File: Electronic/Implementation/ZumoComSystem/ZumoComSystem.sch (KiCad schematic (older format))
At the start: 9 parts, among them J1 Conn_02x13_Odd_Even, J2 USB_A, J3 Conn_02x07_Odd_Even, J4 Conn_02x07_Odd_Even, J5 Conn_02x13_Odd_Even, P1 USB_C_Plug, U1 ESP32-WROOM-32

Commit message: add vertical usb ports (!!!ATTENTION: wrong footprints!!!) only for demonstration
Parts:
- J2: footprint Connector_USB:USB_A_Wuerth_61400826021_Horizontal_Stacked -> footprints:USB_A_Molex_105057_Vertical_2
- P1: footprint Connector_USB:USB_C_Receptacle_GCT_USB4085 -> footprints:USB_C_Receptacle_JAE_DX07S024WJ3R400
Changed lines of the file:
@@
 F 0 "P1" H 9757 3117 50  0000 C CNN
 F 1 "USB_C_Plug" H 9757 3026 50  0000 C CNN
-F 2 "Connector_USB:USB_C_Receptacle_GCT_USB4085" H 9800 1850 50  0001 C CNN
+F 2 "footprints:USB_C_Receptacle_JAE_DX07S024WJ3R400" H 9800 1850 50  0001 C CNN
 F 3 "https://www.usb.org/sites/default/files/documents/usb_type-c.zip" H 9800 1850 50  0001 C CNN
 	1    9650 1850
@@
 F 0 "J2" H 1807 6667 50  0000 C CNN
 F 1 "USB_A" H 1807 6576 50  0000 C CNN
-F 2 "Connector_USB:USB_A_Wuerth_61400826021_Horizontal_Stacked" H 1900 6150 50  0001 C CNN
+F 2 "footprints:USB_A_Molex_105057_Vertical_2" H 1900 6150 50  0001 C CNN
 F 3 " ~" H 1900 6150 50  0001 C CNN
 	1    1750 6200

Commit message: Electronic -> Schematic -> create hierarchical structure, add USB_MAX, add Regulators
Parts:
- removed BT1, BT2: Battery_Cell, footprints:BAT_1043, symbol Device:Battery_Cell
- removed J1, J5: Conn_02x13_Odd_Even, Connector_PinHeader_2.54mm:PinHeader_2x13_P2.54mm_Vertical, symbol Connector_Generic:Conn_02x13_Odd_Even
- removed J2: USB_A, footprints:USB_A_Molex_105057_Vertical_2, symbol Connector:USB_A
- removed J3: Conn_02x07_Odd_Even, Connector_PinSocket_2.54mm:PinSocket_2x07_P2.54mm_Vertical, symbol Connector_Generic:Conn_02x07_Odd_Even
- removed J4: Conn_02x07_Odd_Even, Connector_PinHeader_2.54mm:PinHeader_2x07_P2.54mm_Vertical, symbol Connector_Generic:Conn_02x07_Odd_Even
- removed P1: USB_C_Plug, footprints:USB_C_Receptacle_JAE_DX07S024WJ3R400, symbol Connector:USB_C_Plug
- removed U1: ESP32-WROOM-32, RF_Module:ESP32-WROOM-32, symbol RF_Module:ESP32-WROOM-32
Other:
- note removed: "Display"
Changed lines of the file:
@@
 $Descr A4 11693 8268
 encoding utf-8
-Sheet 1 1
+Sheet 1 7
 Title "Zumo Communication System"
-Date "2021-05-14"
+Date "2021-06-11"
 Rev "V1.0"
 Comp "NewTec GmbH"
-Comment1 "Reyes, Gabryel"
-Comment2 "Schneider, Niklas"
+Comment1 "Schneider, Niklas"
+Comment2 ""
 Comment3 ""
 Comment4 ""
 $EndDescr
-$Comp
-L Connector_Generic:Conn_02x13_Odd_Even J1
-U 1 1 609EB143
-P 1750 4700
-F 0 "J1" H 1800 5517 50  0000 C CNN
-F 1 "Conn_02x13_Odd_Even" H 1800 5426 50  0000 C CNN
-F 2 "Connector_PinHeader_2.54mm:PinHeader_2x13_P2.54mm_Vertical" H 1750 4700 50  0001 C CNN
-F 3 "~" H 1750 4700 50  0001 C CNN
-	1    1750 4700
-	1    0    0    -1
-$EndComp
-$Comp
-L Connector_Generic:Conn_02x13_Odd_Even J5
-U 1 1 609F337D
-P 9750 4700
-F 0 "J5" H 9800 5517 50  0000 C CNN
-F 1 "Conn_02x13_Odd_Even" H 9800 5426 50  0000 C CNN
-F 2 "Connector_PinHeader_2.54mm:PinHeader_2x13_P2.54mm_Vertical" H 9750 4700 50  0001 C CNN
-F 3 "~" H 9750 4700 50  0001 C CNN
-	1    9750 4700
-	1    0    0    -1
-$EndComp
-$Comp
-L Connector_Generic:Conn_02x07_Odd_Even J4
-U 1 1 609FB3EF
-P 5950 2450
-F 0 "J4" V 6046 2062 50  0000 R CNN
-F 1 "Conn_02x07_Odd_Even" V 5955 2062 50  0000 R CNN
-F 2 "Connector_PinHeader_2.54mm:PinHeader_2x07_P2.54mm_Vertical" H 5950 2450 50  0001 C CNN
-F 3 "~" H 5950 2450 50  0001 C CNN
-	1    5950 2450
-	0    -1   -1   0
-$EndComp
-$Comp
-L Connector_Generic:Conn_02x07_Odd_Even J3
-U 1 1 609FDC66
-P 5950 1550
-F 0 "J3" V 6046 1162 50  0000 R CNN
-F 1 "Conn_02x07_Odd_Even" V 5955 1162 50  0000 R CNN
-F 2 "Connector_PinSocket_2.54mm:PinSocket_2x07_P2.54mm_Vertical" H 5950 1550 50  0001 C CNN
-F 3 "~" H 5950 1550 50  0001 C CNN
-	1    5950 1550
-	0    -1   -1   0
-$EndComp
-$Comp
-L RF_Module:ESP32-WROOM-32 U1
-U 1 1 60A02B75
-P 5950 4800
-F 0 "U1" H 5950 6381 50  0000 C CNN
-F 1 "ESP32-WROOM-32" H 5950 6290 50  0000 C CNN
-F 2 "RF_Module:ESP32-WROOM-32" H 5950 3300 50  0001 C CNN
-F 3 "https://www.espressif.com/sites/default/files/documentation/esp32-wroom-32_datasheet_en.pdf" H 5650 4850 50  0001 C CNN
-	1    5950 4800
-	1    0    0    -1
-$EndComp
-$Comp
-L Connector:USB_C_Plug P1
-U 1 1 60A05FF0
-P 9650 1850
-F 0 "P1" H 9757 3117 50  0000 C CNN
-F 1 "USB_C_Plug" H 9757 3026 50  0000 C CNN
-F 2 "footprints:USB_C_Receptacle_JAE_DX07S024WJ3R400" H 9800 1850 50  0001 C CNN
-F 3 "https://www.usb.org/sites/default/files/documents/usb_type-c.zip" H 9800 1850 50  0001 C CNN
-	1    9650 1850
-	1    0    0    -1
-$EndComp
-$Comp
-L Connector:USB_A J2
-U 1 1 60A0D248
-P 1750 6200
-F 0 "J2" H 1807 6667 50  0000 C CNN
-F 1 "USB_A" H 1807 6576 50  0000 C CNN
-F 2 "footprints:USB_A_Molex_105057_Vertical_2" H 1900 6150 50  0001 C CNN
-F 3 " ~" H 1900 6150 50  0001 C CNN
-	1    1750 6200
-	1    0    0    -1
-$EndComp
-Wire Notes Line
-	5450 1150 6500 1150
-Wire Notes Line
-	6500 1150 6500 1850
-Wire Notes Line
-	6500 1850 5450 1850
-Wire Notes Line
-	5450 1850 5450 1150
-Text Notes 5450 1150 0    50   ~ 0
-Display
-$Comp
-L Device:Battery_Cell BT1
-U 1 1 609E86C6
-P 1750 1700
-F 0 "BT1" H 1868 1796 50  0000 L CNN
-F 1 "Battery_Cell" H 1868 1705 50  0000 L CNN
-F 2 "footprints:BAT_1043" V 1750 1760 50  0001 C CNN
-F 3 "~" V 1750 1760 50  0001 C CNN
-	1    1750 1700
-	1    0    0    -1
-$EndComp
-$Comp
-L Device:Battery_Cell BT2
-U 1 1 609E9F71
-P 1750 2150
-F 0 "BT2" H 1868 2246 50  0000 L CNN
-F 1 "Battery_Cell" H 1868 2155 50  0000 L CNN
-F 2 "footprints:BAT_1043" V 1750 2210 50  0001 C CNN
-F 3 "~" V 1750 2210 50  0001 C CNN
-	1    1750 2150
-	1    0    0    -1
-$EndComp
+$Sheet
+S 2750 3800 1500 2500
+U 60C4F1BF
+F0 "Power_Regulation" 50
+F1 "power_reg.sch" 50
+$EndSheet
+$Sheet
+S 6500 800  1500 2500
+U 60C4E4D0
+F0 "ESP" 50
+F1 "ESP.sch" 50
+$EndSheet
+$Sheet
+S 4000 800  1500 2500
+U 60C3F428
+F0 "USB_Power" 50
+F1 "USB_power.sch" 50
+$EndSheet
+$Sheet
+S 6500 3800 1550 2500
+U 60C500E6
+F0 "USB_MAX" 50
+F1 "usb_max.sch" 50
+$EndSheet
+$Sheet
+S 9500 800  950  5500
+U 60C50401
+F0 "IF_Pololu" 50
+F1 "IF_pololu.sch" 50
+$EndSheet
+$Sheet
+S 1500 800  1500 2500
+U 60C3F332
+F0 "Battery" 50
+F1 "battery.sch" 50
+$EndSheet
 $EndSCHEMATC

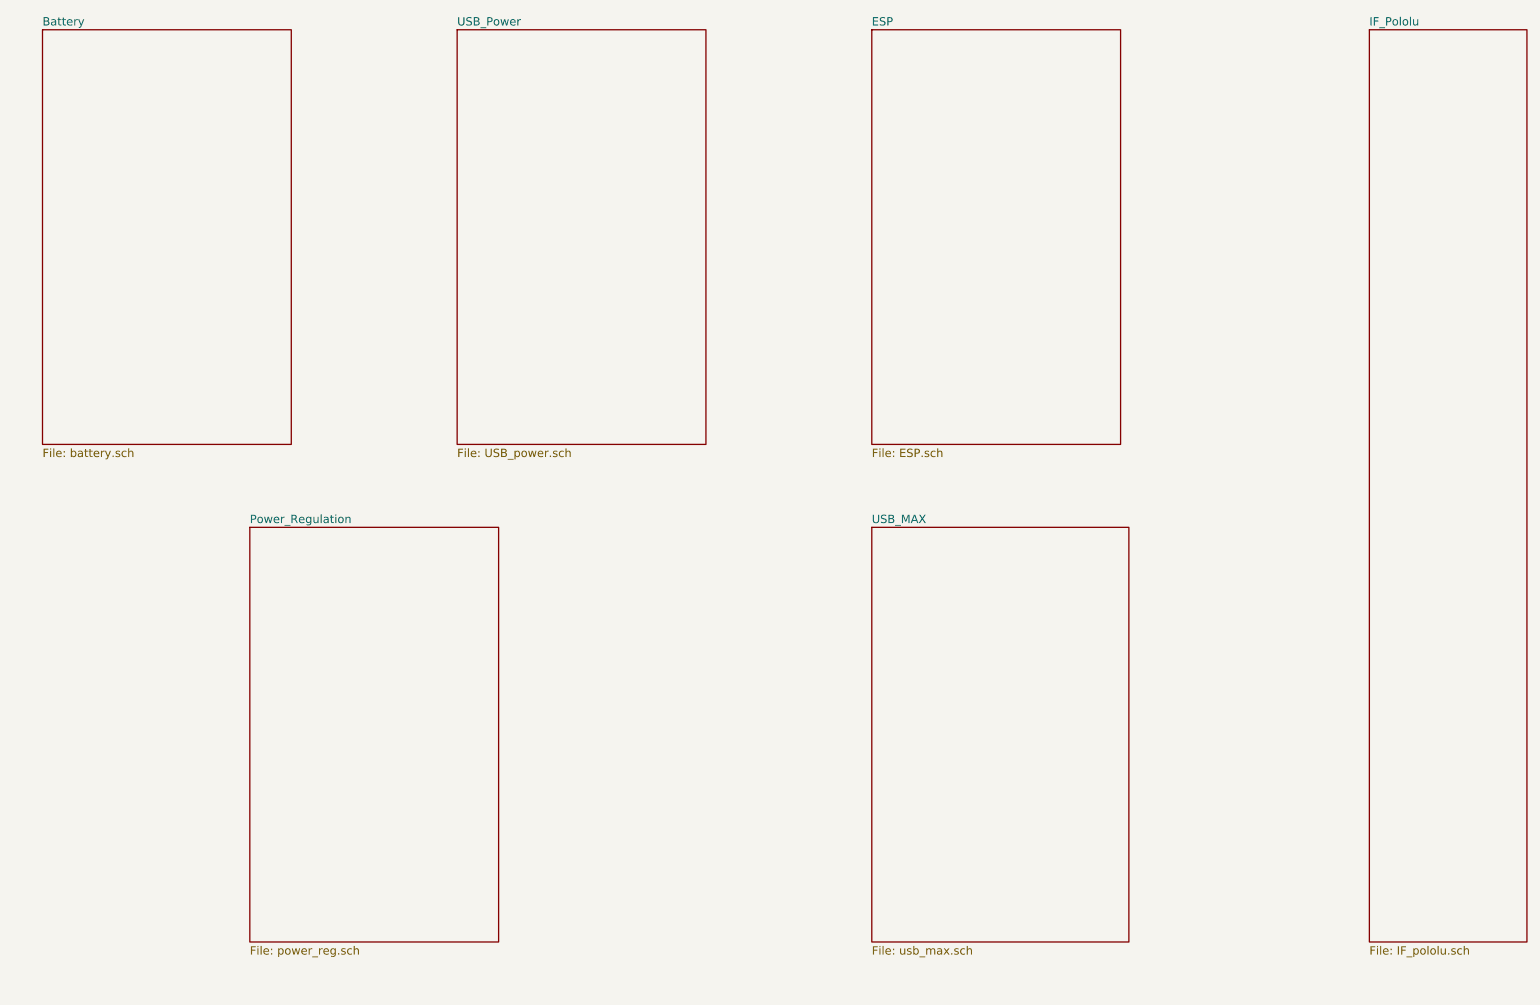
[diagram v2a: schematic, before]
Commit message: electronic -> Schematic -> add hierarchical pins, modified Regulator page
           -> BOM & Clac: add new inductors
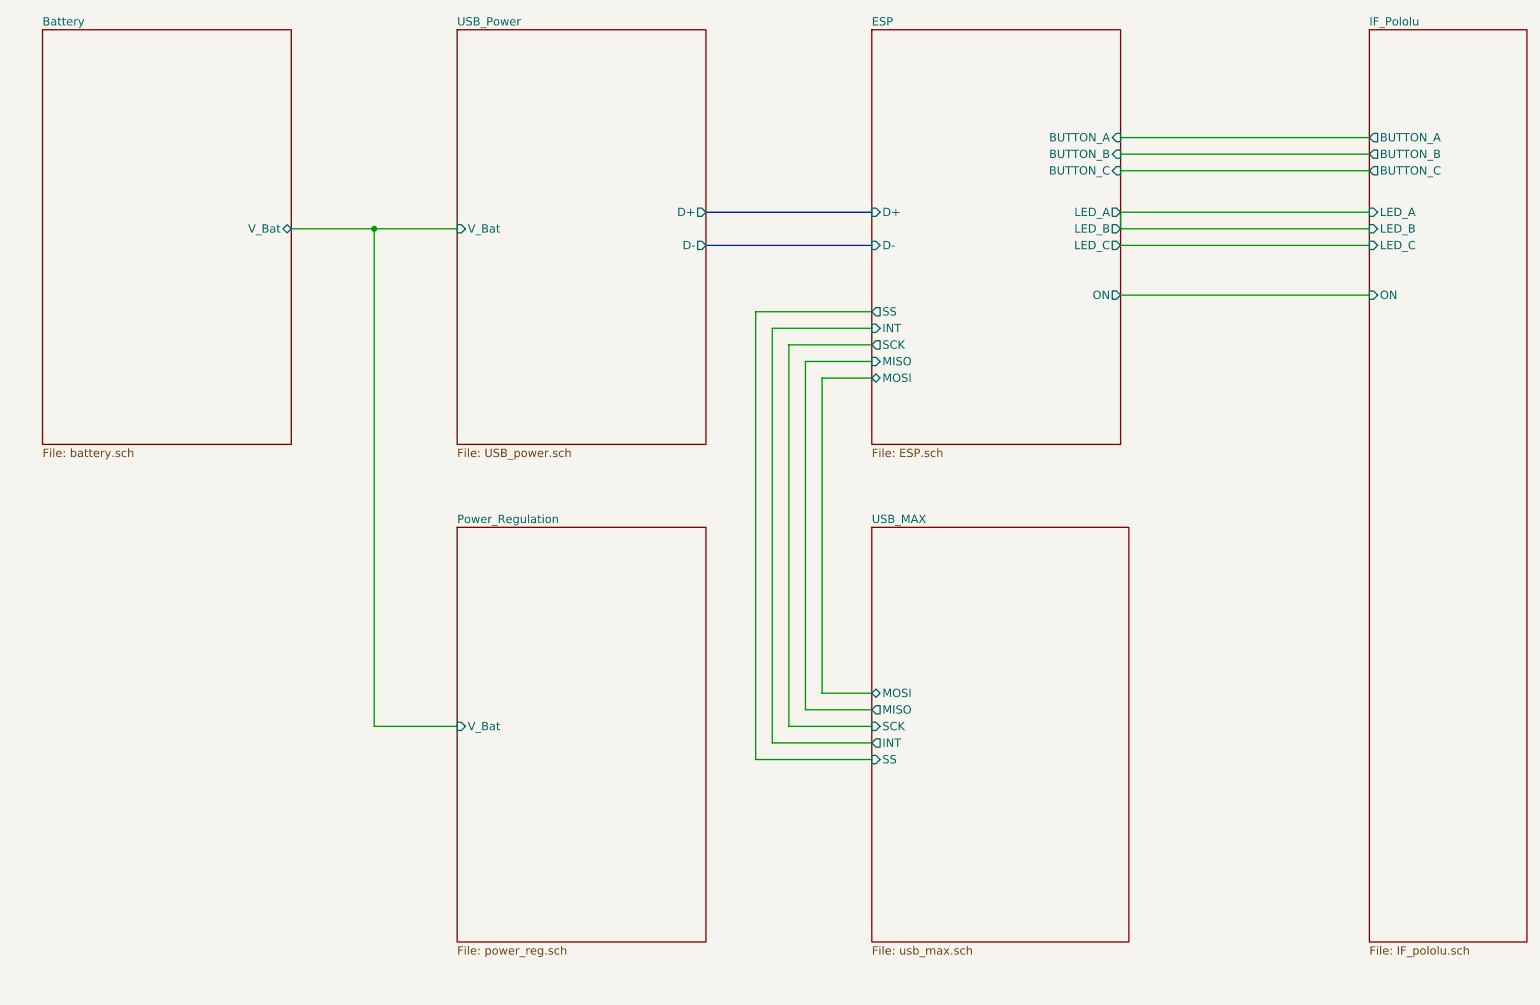
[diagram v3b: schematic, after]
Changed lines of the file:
@@
 $EndDescr
 $Sheet
-S 2750 3800 1500 2500
+S 4000 3800 1500 2500
 U 60C4F1BF
 F0 "Power_Regulation" 50
 F1 "power_reg.sch" 50
+F2 "V_Bat" I L 4000 5000 50
 $EndSheet
 $Sheet
@@
 F0 "ESP" 50
 F1 "ESP.sch" 50
+F2 "D+" I L 6500 1900 50
+F3 "D-" I L 6500 2100 50
+F4 "SS" O L 6500 2500 50
+F5 "INT" I L 6500 2600 50
+F6 "SCK" O L 6500 2700 50
+F7 "MISO" I L 6500 2800 50
+F8 "MOSI" B L 6500 2900 50
+F9 "BUTTON_A" I R 8000 1450 50
+F10 "BUTTON_B" I R 8000 1550 50
+F11 "BUTTON_C" I R 8000 1650 50
+F12 "LED_A" O R 8000 1900 50
+F13 "LED_B" O R 8000 2000 50
+F14 "LED_C" O R 8000 2100 50
+F15 "ON" O R 8000 2400 50
 $EndSheet
 $Sheet
@@
 F0 "USB_Power" 50
 F1 "USB_power.sch" 50
+F2 "V_Bat" I L 4000 2000 50
+F3 "D-" O R 5500 2100 50
+F4 "D+" O R 5500 1900 50
 $EndSheet
 $Sheet
@@
 F0 "USB_MAX" 50
 F1 "usb_max.sch" 50
+F2 "SS" I L 6500 5200 50
+F3 "INT" O L 6500 5100 50
+F4 "SCK" I L 6500 5000 50
+F5 "MISO" O L 6500 4900 50
+F6 "MOSI" B L 6500 4800 50
 $EndSheet
 $Sheet
@@
 F0 "IF_Pololu" 50
 F1 "IF_pololu.sch" 50
+F2 "BUTTON_A" O L 9500 1450 50
+F3 "BUTTON_B" O L 9500 1550 50
+F4 "BUTTON_C" O L 9500 1650 50
+F5 "LED_A" I L 9500 1900 50
+F6 "LED_B" I L 9500 2000 50
+F7 "LED_C" I L 9500 2100 50
+F8 "ON" I L 9500 2400 50
 $EndSheet
 $Sheet
@@
 F0 "Battery" 50
 F1 "battery.sch" 50
+F2 "V_Bat" B R 3000 2000 50
 $EndSheet
+Wire Wire Line
+	3000 2000 3500 2000
+Wire Wire Line
+	3500 2000 3500 5000
+Wire Wire Line
+	3500 5000 4000 5000
+Connection ~ 3500 2000
+Wire Wire Line
+	3500 2000 4000 2000
+Wire Bus Line
+	5500 1900 6500 1900
+Wire Bus Line
+	5500 2100 6500 2100
+Wire Wire Line
+	6500 2500 5800 2500
+Wire Wire Line
+	5800 2500 5800 5200
+Wire Wire Line
+	5800 5200 6500 5200
+Wire Wire Line
+	6500 2600 5900 2600
+Wire Wire Line
+	5900 2600 5900 5100
+Wire Wire Line
+	5900 5100 6500 5100
+Wire Wire Line
+	6500 2700 6000 2700
+Wire Wire Line
+	6000 2700 6000 5000
+Wire Wire Line
+	6000 5000 6500 5000
+Wire Wire Line
+	6500 2800 6100 2800
+Wire Wire Line
+	6100 2800 6100 4900
+Wire Wire Line
+	6100 4900 6500 4900
+Wire Wire Line
+	6500 2900 6200 2900
+Wire Wire Line
+	6200 2900 6200 4800
+Wire Wire Line
+	6200 4800 6500 4800
+Wire Wire Line
+	9500 1450 8000 1450
+Wire Wire Line
+	8000 1550 9500 1550
+Wire Wire Line
+	9500 1650 8000 1650
+Wire Wire Line
+	8000 1900 8000 2000
+Wire Wire Line
+	9500 2000 8000 2000
+Wire Wire Line
+	8000 1900 9500 1900
+Wire Wire Line
+	8000 2100 9500 2100
+Wire Wire Line
+	8000 2400 9500 2400
 $EndSCHEMATC

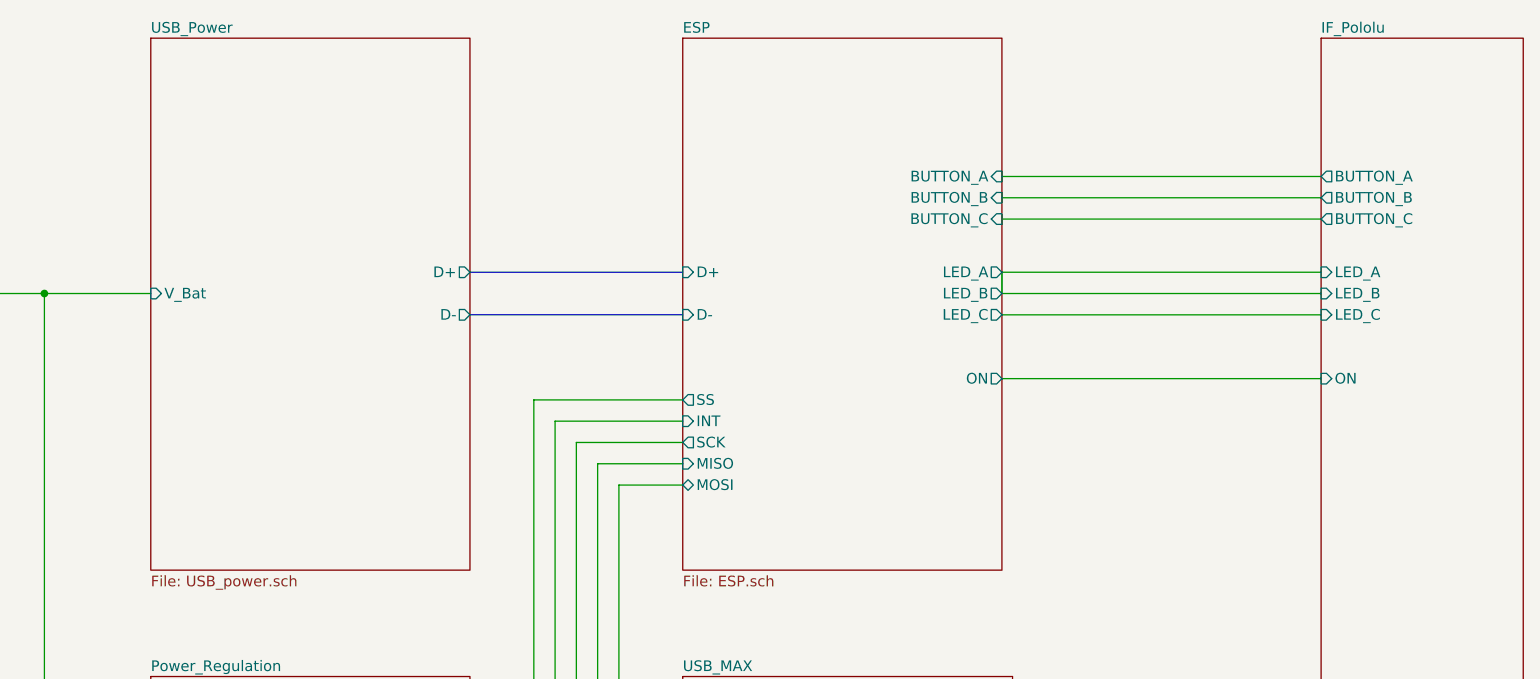
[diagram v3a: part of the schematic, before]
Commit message: Electronic: Schematic: ESP I/Os, IF_Pololu Pins, USB_max
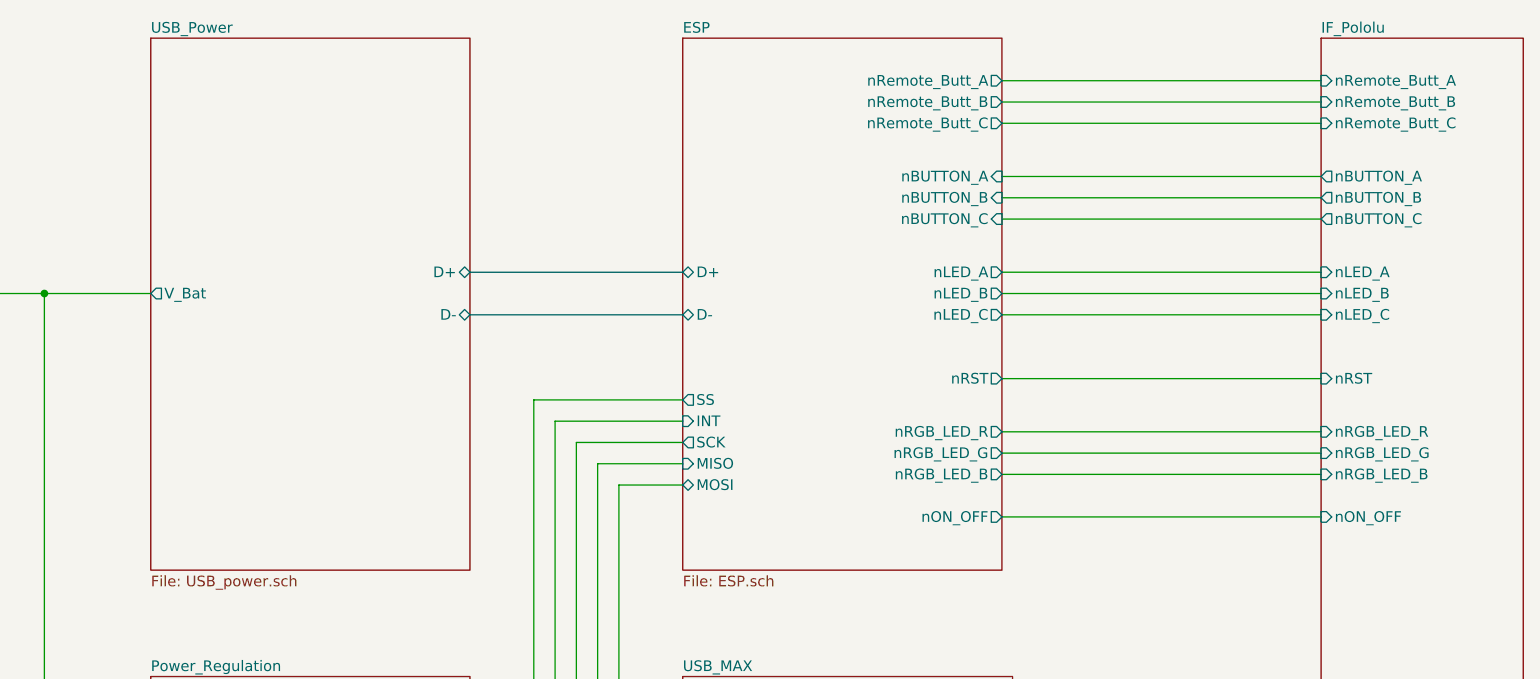
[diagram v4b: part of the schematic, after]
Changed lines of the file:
@@
 Sheet 1 7
 Title "Zumo Communication System"
-Date "2021-06-11"
+Date "2021-07-28"
 Rev "V1.0"
 Comp "NewTec GmbH"
@@
 $EndSheet
 $Sheet
-S 6500 800  1500 2500
-U 60C4E4D0
-F0 "ESP" 50
-F1 "ESP.sch" 50
-F2 "D+" I L 6500 1900 50
-F3 "D-" I L 6500 2100 50
-F4 "SS" O L 6500 2500 50
-F5 "INT" I L 6500 2600 50
-F6 "SCK" O L 6500 2700 50
-F7 "MISO" I L 6500 2800 50
-F8 "MOSI" B L 6500 2900 50
-F9 "BUTTON_A" I R 8000 1450 50
-F10 "BUTTON_B" I R 8000 1550 50
-F11 "BUTTON_C" I R 8000 1650 50
-F12 "LED_A" O R 8000 1900 50
-F13 "LED_B" O R 8000 2000 50
-F14 "LED_C" O R 8000 2100 50
-F15 "ON" O R 8000 2400 50
-$EndSheet
-$Sheet
-S 4000 800  1500 2500
-U 60C3F428
-F0 "USB_Power" 50
-F1 "USB_power.sch" 50
-F2 "V_Bat" I L 4000 2000 50
-F3 "D-" O R 5500 2100 50
-F4 "D+" O R 5500 1900 50
-$EndSheet
-$Sheet
 S 6500 3800 1550 2500
 U 60C500E6
@@
 F5 "MISO" O L 6500 4900 50
 F6 "MOSI" B L 6500 4800 50
-$EndSheet
-$Sheet
-S 9500 800  950  5500
-U 60C50401
-F0 "IF_Pololu" 50
-F1 "IF_pololu.sch" 50
-F2 "BUTTON_A" O L 9500 1450 50
-F3 "BUTTON_B" O L 9500 1550 50
-F4 "BUTTON_C" O L 9500 1650 50
-F5 "LED_A" I L 9500 1900 50
-F6 "LED_B" I L 9500 2000 50
-F7 "LED_C" I L 9500 2100 50
-F8 "ON" I L 9500 2400 50
 $EndSheet
 $Sheet
@@
 	9500 1650 8000 1650
 Wire Wire Line
-	8000 1900 8000 2000
-Wire Wire Line
 	9500 2000 8000 2000
 Wire Wire Line
@@
 Wire Wire Line
 	8000 2400 9500 2400
+$Sheet
+S 4000 800  1500 2500
+U 60C3F428
+F0 "USB_Power" 50
+F1 "USB_power.sch" 50
+F2 "V_Bat" O L 4000 2000 50
+F3 "D-" B R 5500 2100 50
+F4 "D+" B R 5500 1900 50
+$EndSheet
+$Sheet
+S 9500 800  950  5500
+U 60C50401
+F0 "IF_Pololu" 50
+F1 "IF_pololu.sch" 50
+F2 "nLED_B" I L 9500 2000 50
+F3 "nLED_C" I L 9500 2100 50
+F4 "nLED_A" I L 9500 1900 50
+F5 "nBUTTON_B" O L 9500 1550 50
+F6 "nBUTTON_C" O L 9500 1650 50
+F7 "nBUTTON_A" O L 9500 1450 50
+F8 "nRGB_LED_R" I L 9500 2650 50
+F9 "nRGB_LED_G" I L 9500 2750 50
+F10 "nRGB_LED_B" I L 9500 2850 50
+F11 "nRemote_Butt_A" I L 9500 1000 50
+F12 "nRemote_Butt_B" I L 9500 1100 50
+F13 "nRemote_Butt_C" I L 9500 1200 50
+F14 "nRST" I L 9500 2400 50
+F15 "nON_OFF" I L 9500 3050 50
+$EndSheet
+Wire Wire Line
+	8000 2650 9500 2650
+Wire Wire Line
+	8000 2750 9500 2750
+Wire Wire Line
+	8000 2850 9500 2850
+$Sheet
+S 6500 800  1500 2500
+U 60C4E4D0
+F0 "ESP" 50
+F1 "ESP.sch" 50
+F2 "SS" O L 6500 2500 50
+F3 "INT" I L 6500 2600 50
+F4 "SCK" O L 6500 2700 50
+F5 "MISO" I L 6500 2800 50
+F6 "MOSI" B L 6500 2900 50
+F7 "D+" B L 6500 1900 50
+F8 "D-" B L 6500 2100 50
+F9 "nBUTTON_A" I R 8000 1450 50
+F10 "nBUTTON_B" I R 8000 1550 50
+F11 "nBUTTON_C" I R 8000 1650 50
+F12 "nLED_A" O R 8000 1900 50
+F13 "nLED_B" O R 8000 2000 50
+F14 "nLED_C" O R 8000 2100 50
+F15 "nRGB_LED_R" O R 8000 2650 50
+F16 "nRGB_LED_G" O R 8000 2750 50
+F17 "nRGB_LED_B" O R 8000 2850 50
+F18 "nRST" O R 8000 2400 50
+F19 "nRemote_Butt_A" O R 8000 1000 50
+F20 "nRemote_Butt_B" O R 8000 1100 50
+F21 "nRemote_Butt_C" O R 8000 1200 50
+F22 "nON_OFF" O R 8000 3050 50
+$EndSheet
+Wire Wire Line
+	9500 1000 8000 1000
+Wire Wire Line
+	8000 1100 9500 1100
+Wire Wire Line
+	9500 1200 8000 1200
+Wire Wire Line
+	9500 3050 8000 3050
 $EndSCHEMATC
